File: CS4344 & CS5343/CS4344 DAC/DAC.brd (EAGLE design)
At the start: 28 x 16 mm, 22 parts

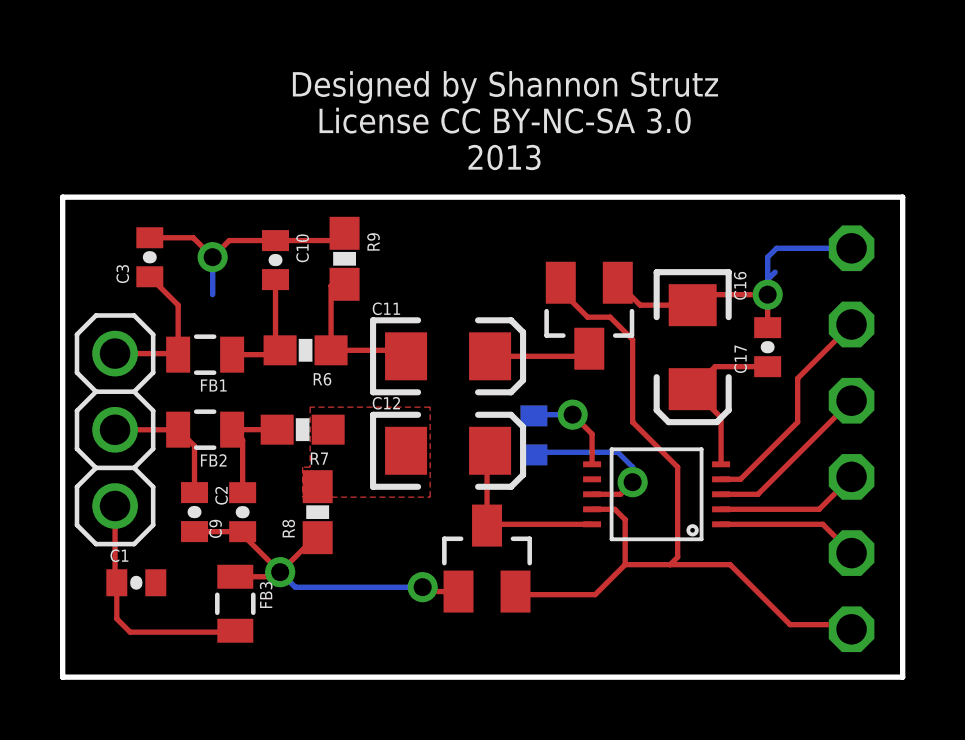
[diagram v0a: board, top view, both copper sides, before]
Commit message: Update DAC,ADC, and ADSP
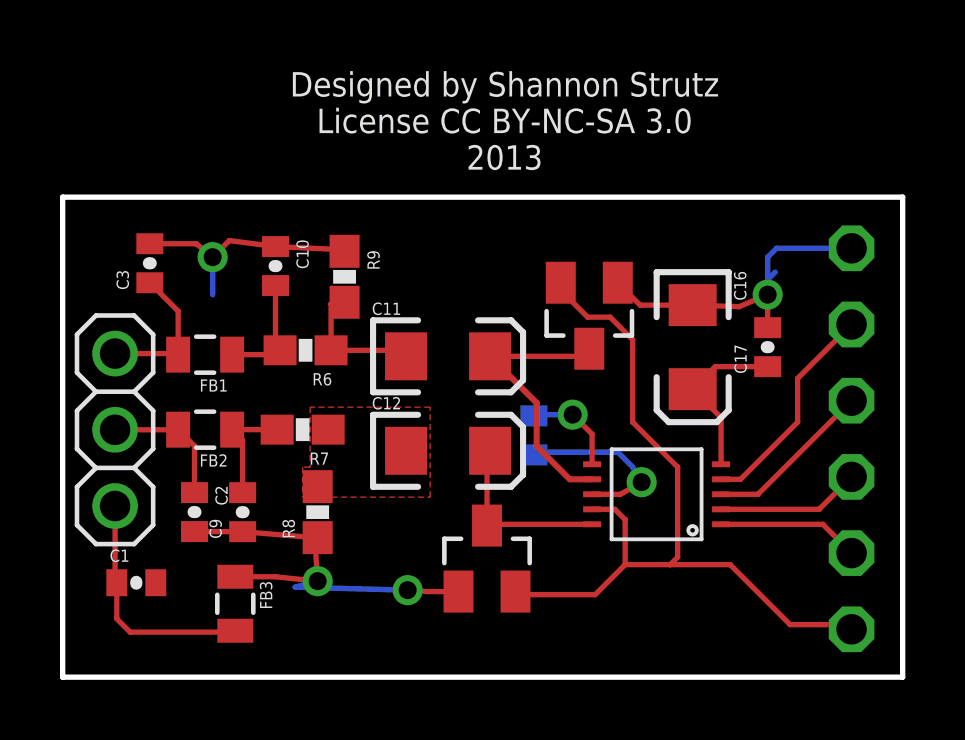
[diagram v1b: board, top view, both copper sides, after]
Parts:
- moved R9 0.60 mm to (9.40, 13.3)
- moved C10 0.20 mm to (7.10, 13.7)
- moved C3 0.20 mm to (2.90, 13.8)
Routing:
- net AOUTL_C: track 3.41 -> 9.36 mm
- net GND: track 38.4 -> 40.1 mm
- net AOUTL_R: track 5.19 -> 4.59 mm
- added copper zone on layer 1, net GND
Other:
- board text added: "CS4344 24-bit I2S DAC Evaluation Shannon Strutz"
- board text removed: "CS4344 24-bit I2S DAC EVM Shannon Strutz"
